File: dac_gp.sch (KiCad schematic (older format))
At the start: 7 parts, among them U10 TMUX6136PWR, U11 TMUX6136PWR, U5 DAC80508ZRTER

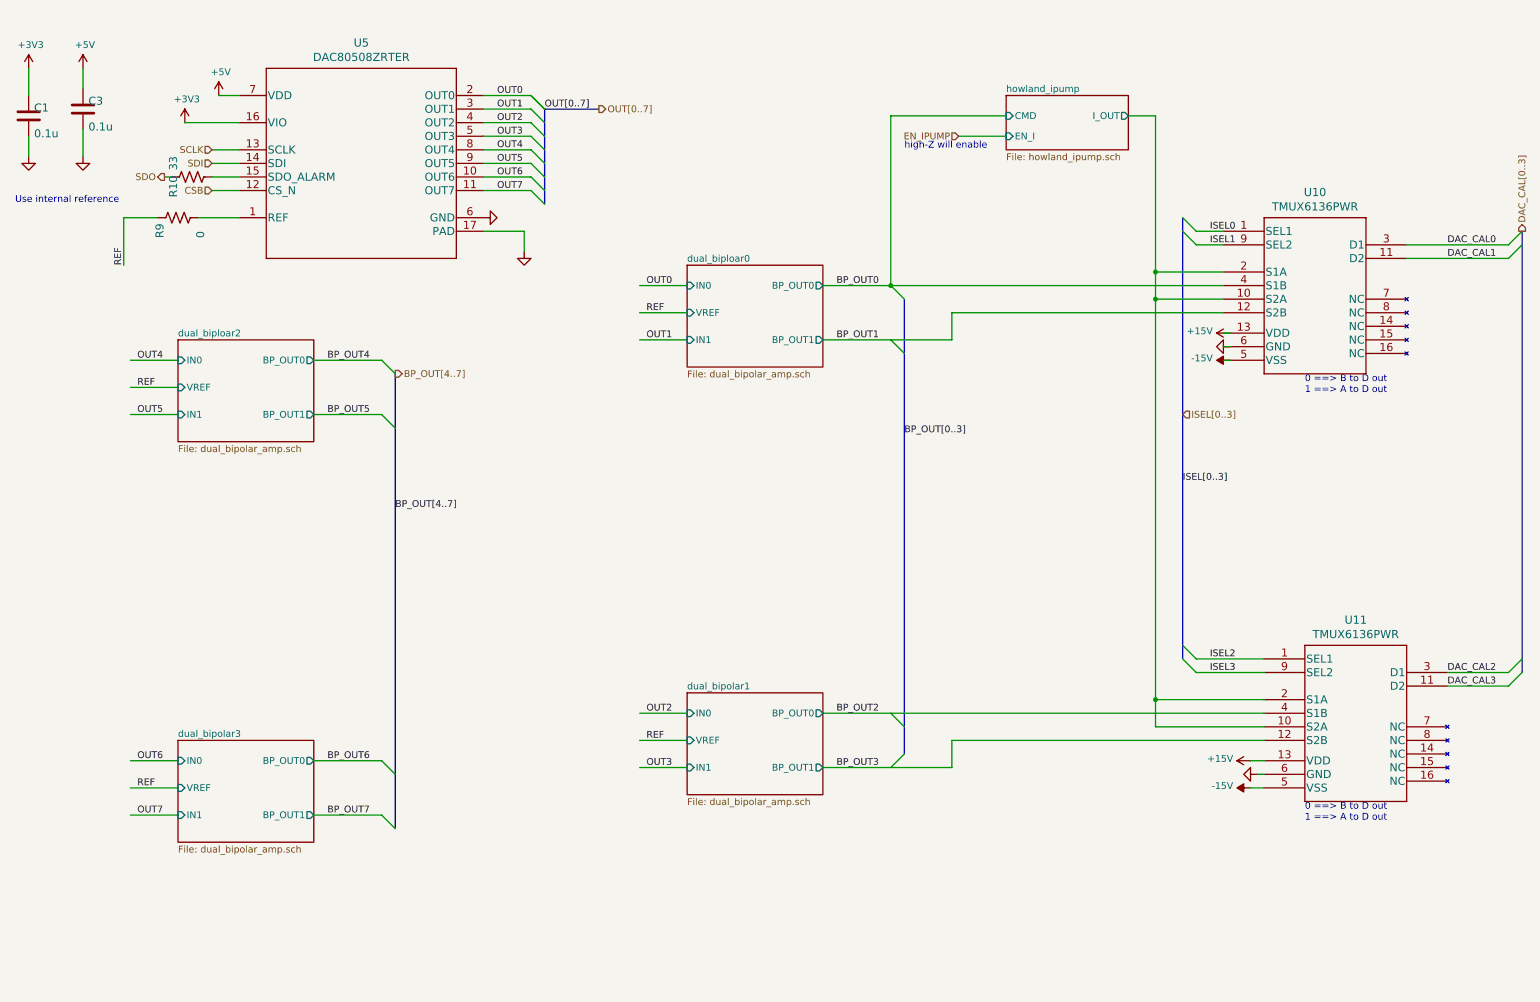
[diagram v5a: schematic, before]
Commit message: updates after bug in ADS8686 power connectivity. And swap of DC SCL and SDA
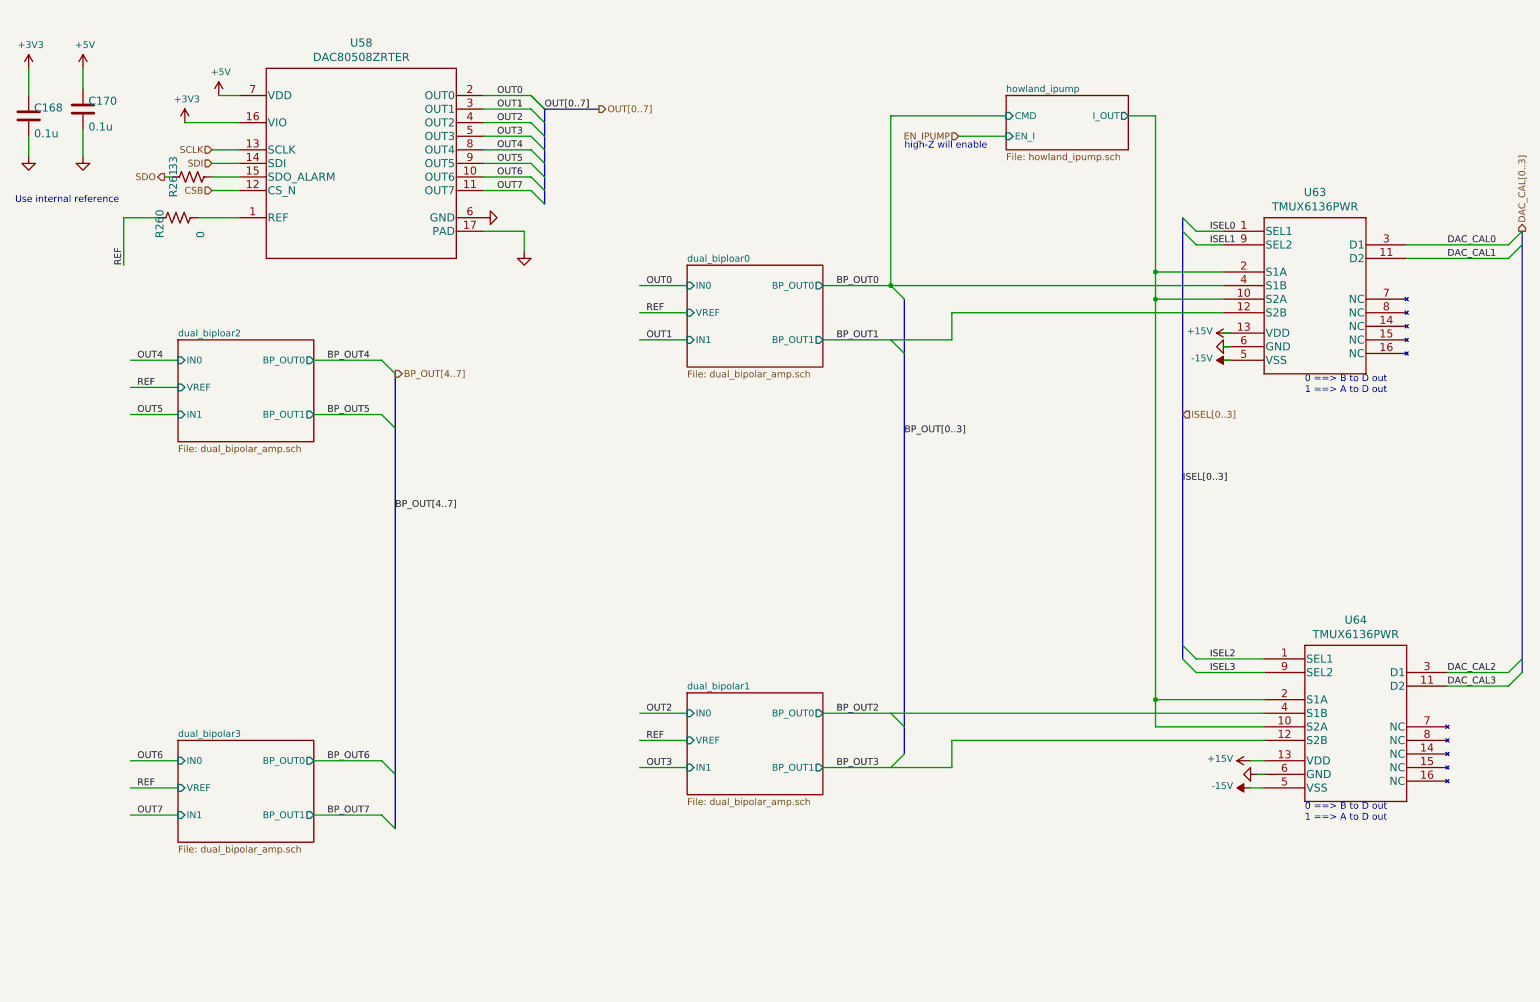
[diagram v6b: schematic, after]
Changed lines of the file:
@@
 AR Path="/6095BD4C/519C2D15" Ref="#FRAME1"  Part="1"
 AR Path="/61B02572/519C2D15" Ref="#FRAME2"  Part="1"
-F 0 "#FRAME1" H 900 6900 50  0001 C CNN
+F 0 "#FRAME2" H 900 6900 50  0001 C CNN
 F 1 "FRAME_A_L" H 900 6900 50  0001 C CNN
 F 2 "" H 900 6900 50  0001 C CNN
@@
 AR Path="/6095BD4C/A7A1DCDA" Ref="C1"  Part="1"
 AR Path="/61B02572/A7A1DCDA" Ref="C168"  Part="1"
-F 0 "C1" H 690 1275 59  0000 L BNN
+F 0 "C168" H 690 1275 59  0000 L BNN
 F 1 "0.1u" H 690 1085 59  0000 L BNN
 F 2 "Capacitor_SMD:C_0603_1608Metric" H 650 1250 50  0001 C CNN
@@
 AR Path="/6095BD4C/46ACB443" Ref="C3"  Part="1"
 AR Path="/61B02572/46ACB443" Ref="C170"  Part="1"
-F 0 "C3" H 1090 1225 59  0000 L BNN
+F 0 "C170" H 1090 1225 59  0000 L BNN
 F 1 "0.1u" H 1090 1035 59  0000 L BNN
 F 2 "Capacitor_SMD:C_0603_1608Metric" H 1050 1200 50  0001 C CNN
@@
 AR Path="/6095BD4C/60A11E5A" Ref="U5"  Part="1"
 AR Path="/61B02572/60A11E5A" Ref="U58"  Part="1"
-F 0 "U5" H 3100 2488 60  0000 C CNN
+F 0 "U58" H 3100 2488 60  0000 C CNN
 F 1 "DAC80508ZRTER" H 3100 2382 60  0000 C CNN
 F 2 "Package_DFN_QFN:WQFN-16-1EP_3x3mm_P0.5mm_EP1.6x1.6mm" H 3100 1540 60  0001 C CNN
@@
 AR Path="/6095BD4C/60A29EE1" Ref="R9"  Part="1"
 AR Path="/61B02572/60A29EE1" Ref="R260"  Part="1"
-F 0 "R9" H 1600 2100 59  0000 L BNN
+F 0 "R260" H 1600 2100 59  0000 L BNN
 F 1 "0" H 1600 1800 59  0000 L BNN
 F 2 "Resistor_SMD:R_0603_1608Metric" H 1750 2000 50  0001 C CNN
@@
 AR Path="/6095BD4C/60B8C0FB" Ref="U10"  Part="1"
 AR Path="/61B02572/60B8C0FB" Ref="U63"  Part="1"
-F 0 "U10" H 10125 2387 60  0000 C CNN
+F 0 "U63" H 10125 2387 60  0000 C CNN
 F 1 "TMUX6136PWR" H 10125 2281 60  0000 C CNN
 F 2 "Package_SO:TSSOP-16_4.4x5mm_P0.65mm" H 10100 2200 60  0001 C CNN
@@
 AR Path="/6095BD4C/60C5A3EA" Ref="U11"  Part="1"
 AR Path="/61B02572/60C5A3EA" Ref="U64"  Part="1"
-F 0 "U11" H 10425 5537 60  0000 C CNN
+F 0 "U64" H 10425 5537 60  0000 C CNN
 F 1 "TMUX6136PWR" H 10425 5431 60  0000 C CNN
 F 2 "Package_SO:TSSOP-16_4.4x5mm_P0.65mm" H 10400 5350 60  0001 C CNN
@@
 AR Path="/6095BD4C/617C87E1" Ref="R10"  Part="1"
 AR Path="/61B02572/617C87E1" Ref="R261"  Part="1"
-F 0 "R10" H 1700 1800 59  0000 L BNN
+F 0 "R261" H 1700 1800 59  0000 L BNN
 F 1 "33" H 1900 1800 59  0000 L BNN
 F 2 "Resistor_SMD:R_0603_1608Metric" H 1850 1700 50  0001 C CNN
@@
 Wire Wire Line
 	9450 2700 7450 2700
-Wire Bus Line
-	7100 2600 7100 5950
 Text Label 7100 3600 0    50   ~ 0
 BP_OUT[0..3]
@@
 	3350 3150 3350 6500
 Wire Bus Line
+	7100 2600 7100 5950
+Wire Bus Line
 	4450 1200 4450 1900
